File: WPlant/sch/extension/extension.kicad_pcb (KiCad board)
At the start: 2 copper layers, 73 x 50 mm, 45 parts, among them J1 PROG/SWD, J2 HumSnc, J3 HumSnc, J4 HumSnc, J5 HumSnc, J6 Input, J7 Output, J8 LeakDetect, J9 Valves, Q1 FDS9926A, Q2 FDS9926A, U1 PY32F003F18P6TU, U2 74HC594, U3 74HC4052, U4 SP485EEN-L/TR, U6 AP2204R-5.0, U7 SP485EEN-L/TR

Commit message: Update WP Extension and Generic
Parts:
- added C10: 100, Capacitor_THT:CP_Radial_D5.0mm_P2.00mm, F.Cu at (189.5, 61.6)
- added C9: NP, Capacitor_SMD:C_1206_3216Metric_Pad1.33x1.80mm_HandSolder, F.Cu at (191.1, 76.8)
- added R11: 100, Resistor_SMD:R_0603_1608Metric_Pad0.98x0.95mm_HandSolder, F.Cu at (151.1, 62.2)
- moved H4 19.5 mm to (171.6, 61.3)
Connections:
- U3 pad 13: +5V -> Net-(U3-X)
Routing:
- net Net-(U3-X): track 0.00 -> 8.68 mm
- net +9V: track 144.8 -> 148.5 mm
- net /F4: track 22.6 -> 25.2 mm
- net GND: track 69.5 -> 71.7 mm, vias 173 -> 165
- net +5V: track 215.5 -> 214.5 mm
- net /P4: track 23.8 -> 23.3 mm

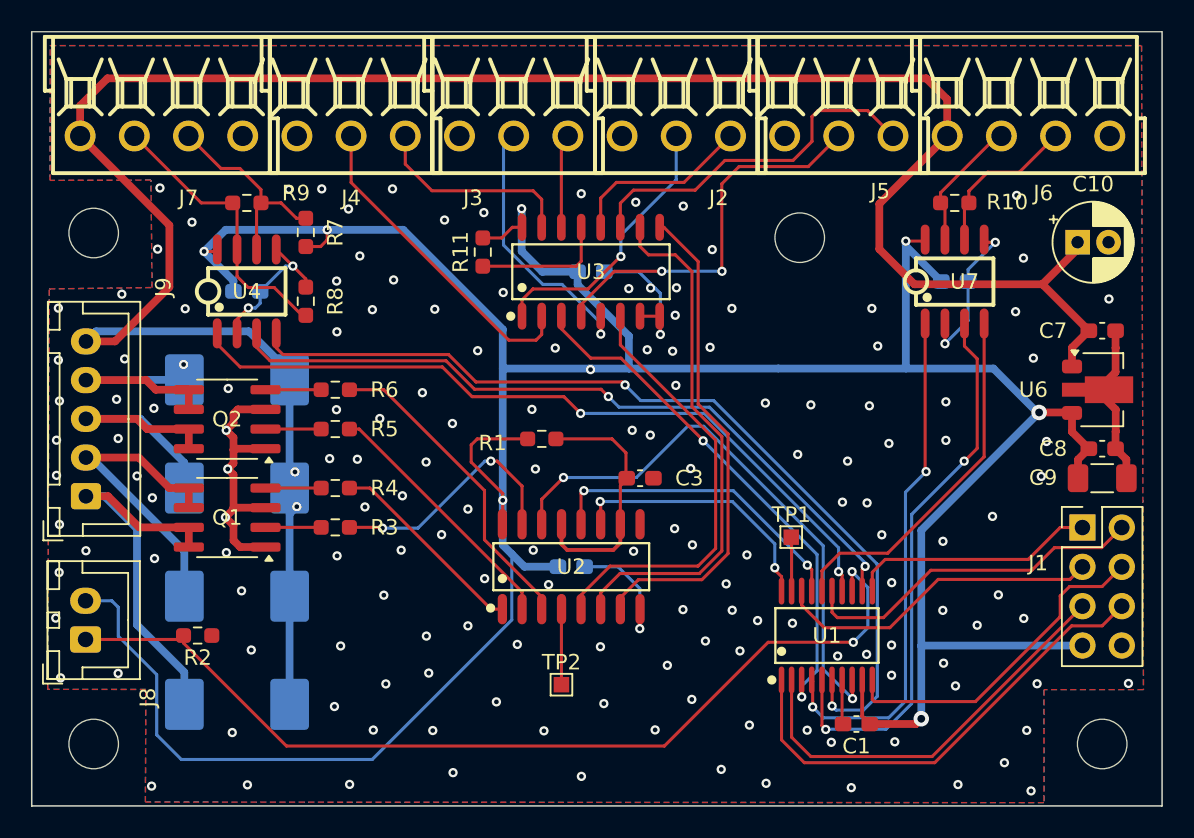
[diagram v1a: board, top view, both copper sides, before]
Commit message: Addeed places for latches on Extension board. Updated MainInt sch and pcb
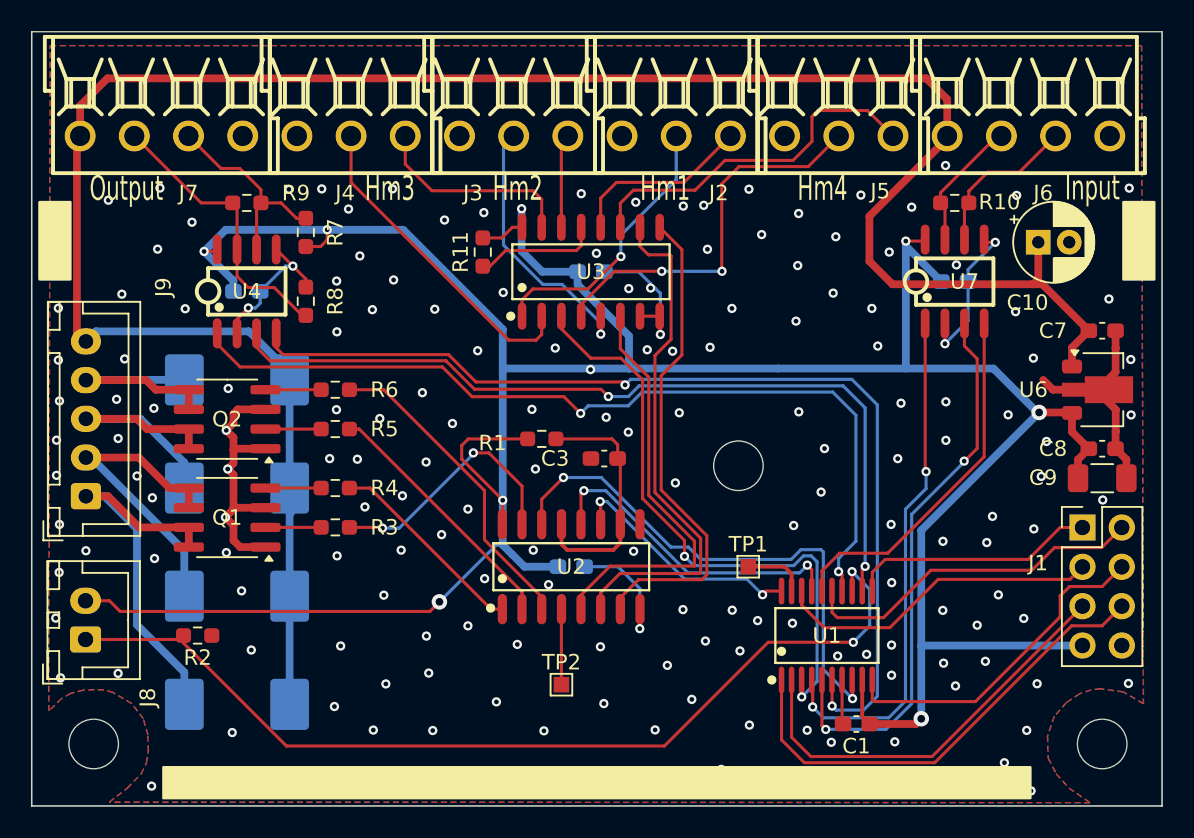
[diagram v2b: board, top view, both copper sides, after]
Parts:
- removed H3: M3, MountingHole:MountingHole_3.2mm_M3
- moved H4 15.3 mm to (167.6, 76.0)
- moved TP1 3.37 mm to (168.3, 82.5)
- moved C3 2.64 mm to (159.0, 75.6), turned to 180 degrees
- moved C10 2.54 mm to (187.0, 61.6)
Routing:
- net +5V: track 214.5 -> 201.2 mm, vias 8 -> 9
- net Net-(U1-PB7): track 49.2 -> 56.9 mm
- net Net-(U1-PB5): track 47.9 -> 54.3 mm
- net Net-(U1-PA7): track 59.2 -> 65.5 mm
- net FREQ-OUT: track 34.1 -> 39.4 mm
- net +9V: track 148.5 -> 143.7 mm, vias 2 -> 0
- net Net-(U1-PA12): track 36.8 -> 34.4 mm
- net GND: track 71.7 -> 73.9 mm, vias 165 -> 179
- net Net-(U1-PA1): track 17.1 -> 15.8 mm
- net Net-(U2-QF): track 28.4 -> 27.1 mm
- net Net-(U3-X): track 8.68 -> 8.11 mm
- net Net-(U1-PA0): track 3.59 -> 4.11 mm
- net Net-(D4-A): vias 1 -> 0
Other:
- board text added: "Hm1"
- board text added: "Hm2"
- board text added: "Hm3"
- board text added: "Hm4"
- board text added: "Input"
- board text added: "Output"

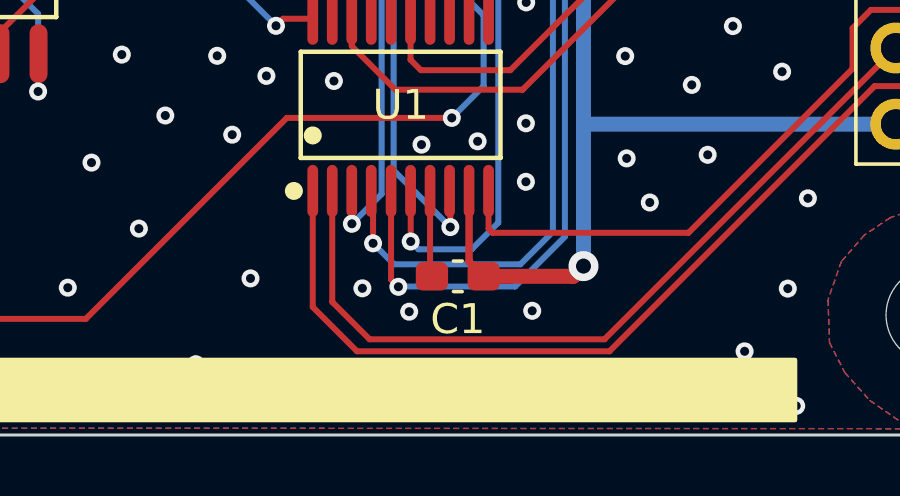
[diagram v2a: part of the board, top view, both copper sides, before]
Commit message: Updated PCB for extension and powermeter
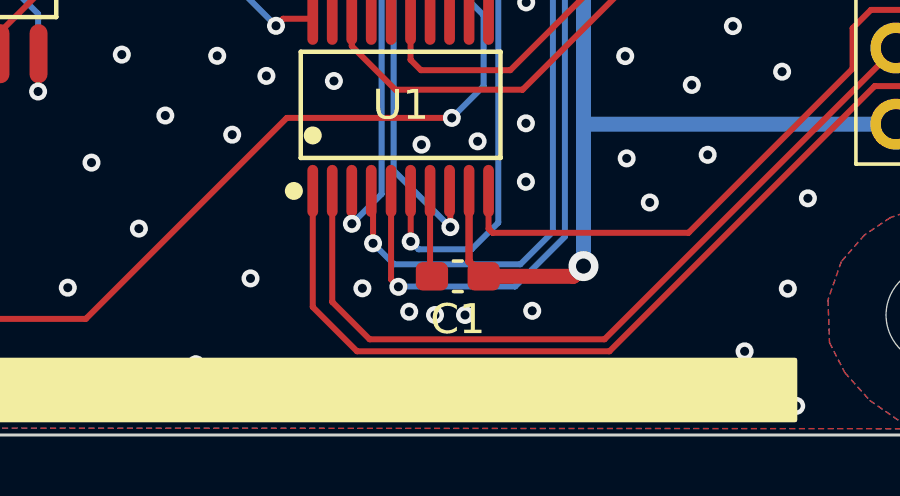
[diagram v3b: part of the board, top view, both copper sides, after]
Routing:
- net GND: vias 179 -> 181
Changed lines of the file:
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@@
+	)
+	(via
+		(at 175.5 94)
+		(size 0.6)
+		(drill 0.3)
+		(layers "F.Cu" "B.Cu")
+		(free yes)
+		(net 1)
 	)
 	(via
@@
 		(size 0.6)
 		(drill 0.3)
+		(layers "F.Cu" "B.Cu")
+		(free yes)
+		(net 1)
+	)
+	(via
+		(at 174.5 94)
+		(size 0.6)
+		(drill 0.3)

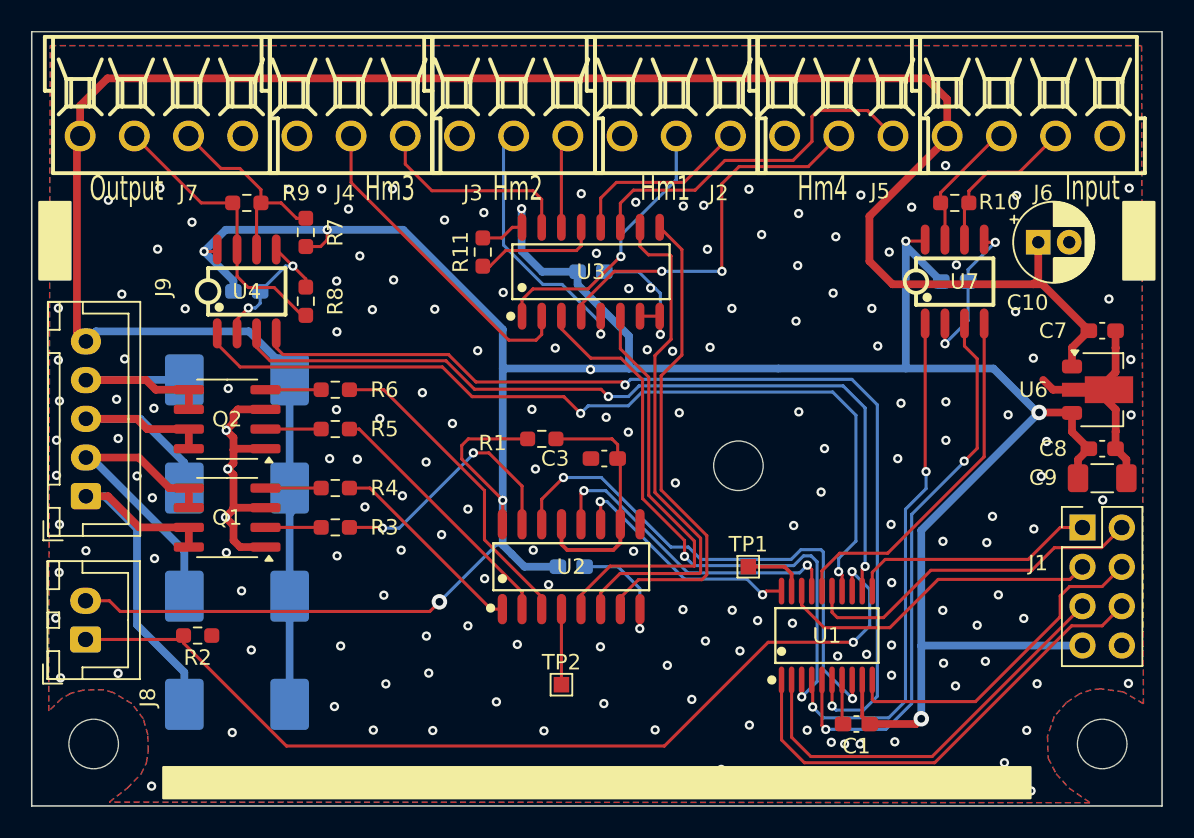
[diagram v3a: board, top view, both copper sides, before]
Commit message: Route of WP project done
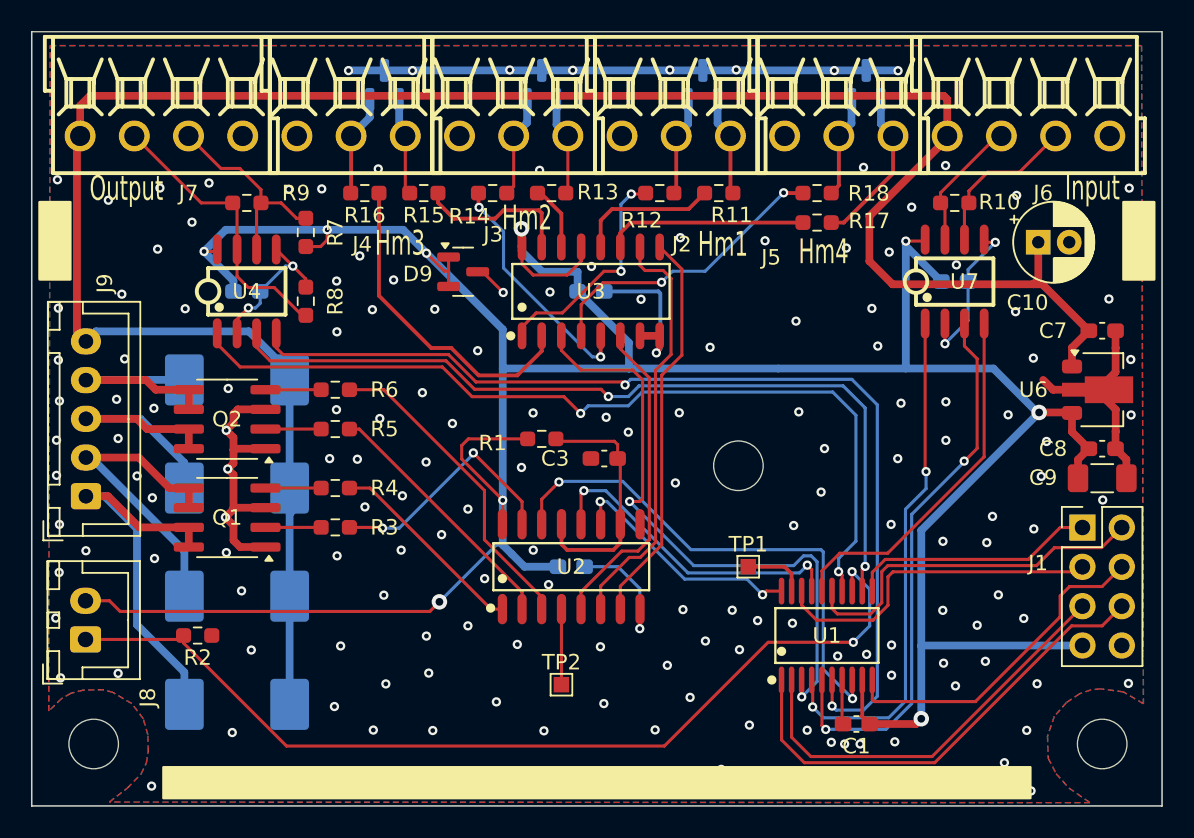
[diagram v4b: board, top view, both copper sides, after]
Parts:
- added D5: MMBZ5V6, Package_TO_SOT_SMD:SOT-23, B.Cu at (175.9, 51.4)
- added D6: MMBZ5V6, Package_TO_SOT_SMD:SOT-23, B.Cu at (144.8, 51.4)
- added D7: MMBZ5V6, Package_TO_SOT_SMD:SOT-23, B.Cu at (154.9, 51.4)
- added D8: MMBZ5V6, Package_TO_SOT_SMD:SOT-23, B.Cu at (165.3, 51.4)
- added D9: MMBZ5V6, Package_TO_SOT_SMD:SOT-23, F.Cu at (149.9, 63.5)
- added R12: 100, Resistor_SMD:R_0603_1608Metric_Pad0.98x0.95mm_HandSolder, F.Cu at (162.6, 58.4)
- added R13: 100, Resistor_SMD:R_0603_1608Metric_Pad0.98x0.95mm_HandSolder, F.Cu at (155.6, 58.4)
- added R14: 100, Resistor_SMD:R_0603_1608Metric_Pad0.98x0.95mm_HandSolder, F.Cu at (151.8, 58.4)
- added R15: 100, Resistor_SMD:R_0603_1608Metric_Pad0.98x0.95mm_HandSolder, F.Cu at (147.3, 58.4)
- added R16: 100, Resistor_SMD:R_0603_1608Metric_Pad0.98x0.95mm_HandSolder, F.Cu at (143.5, 58.4)
- added R17: 100, Resistor_SMD:R_0603_1608Metric_Pad0.98x0.95mm_HandSolder, F.Cu at (172.7, 60.3)
- added R18: 100, Resistor_SMD:R_0603_1608Metric_Pad0.98x0.95mm_HandSolder, F.Cu at (172.7, 58.4)
- moved R11 15.7 mm to (166.4, 58.4), turned to 0 degrees
- moved C4 1.27 mm to (158.1, 64.8)
- moved U3 1.27 mm to (158.1, 64.8)
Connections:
- J2 pad 1: /P1 -> Net-(J2-Pin_1)
- J2 pad 2: /F1 -> Net-(J2-Pin_2)
- J3 pad 1: /P2 -> Net-(J3-Pin_1)
- J3 pad 2: /F2 -> Net-(J3-Pin_2)
- J4 pad 1: /P3 -> Net-(J4-Pin_1)
- J4 pad 2: /F3 -> Net-(J4-Pin_2)
- J5 pad 1: /P4 -> Net-(J5-Pin_1)
- J5 pad 2: /F4 -> Net-(J5-Pin_2)
- R11 pad 1: Net-(U3-X) -> /P1
- R11 pad 2: +5V -> Net-(J2-Pin_1)
- U3 pad 13: Net-(U3-X) -> +5V
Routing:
- net GND: track 73.9 -> 112.4 mm, vias 181 -> 175
- net Net-(J5-Pin_1): track 0.00 -> 10.4 mm
- net /P4: track 23.3 -> 13.0 mm
- net Net-(U3-X): track 8.11 -> 0.00 mm
- net Net-(J3-Pin_2): track 0.00 -> 7.52 mm
- net Net-(J3-Pin_1): track 0.00 -> 7.00 mm
- net Net-(J5-Pin_2): track 0.00 -> 6.59 mm
- net Net-(J4-Pin_2): track 0.00 -> 6.56 mm
- net Net-(J2-Pin_1): track 0.00 -> 6.46 mm
- net Net-(J2-Pin_2): track 0.00 -> 6.43 mm
- net Net-(U2-QG): track 33.6 -> 27.2 mm
- net Net-(J4-Pin_1): track 0.00 -> 6.33 mm
- net Net-(U2-QF): track 27.1 -> 20.9 mm
- net +5V: track 201.2 -> 207.4 mm
- net Net-(U2-QH): track 31.7 -> 25.6 mm
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
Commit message: Added connectors marks on back of PCBs
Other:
- board text added: "+"
- board text added: "-"
- board text added: "1"
- board text added: "2"
- board text added: "3"
- board text added: "4"
- board text added: "A"
- board text added: "B"
- board text added: "In"
- board text added: "Out"

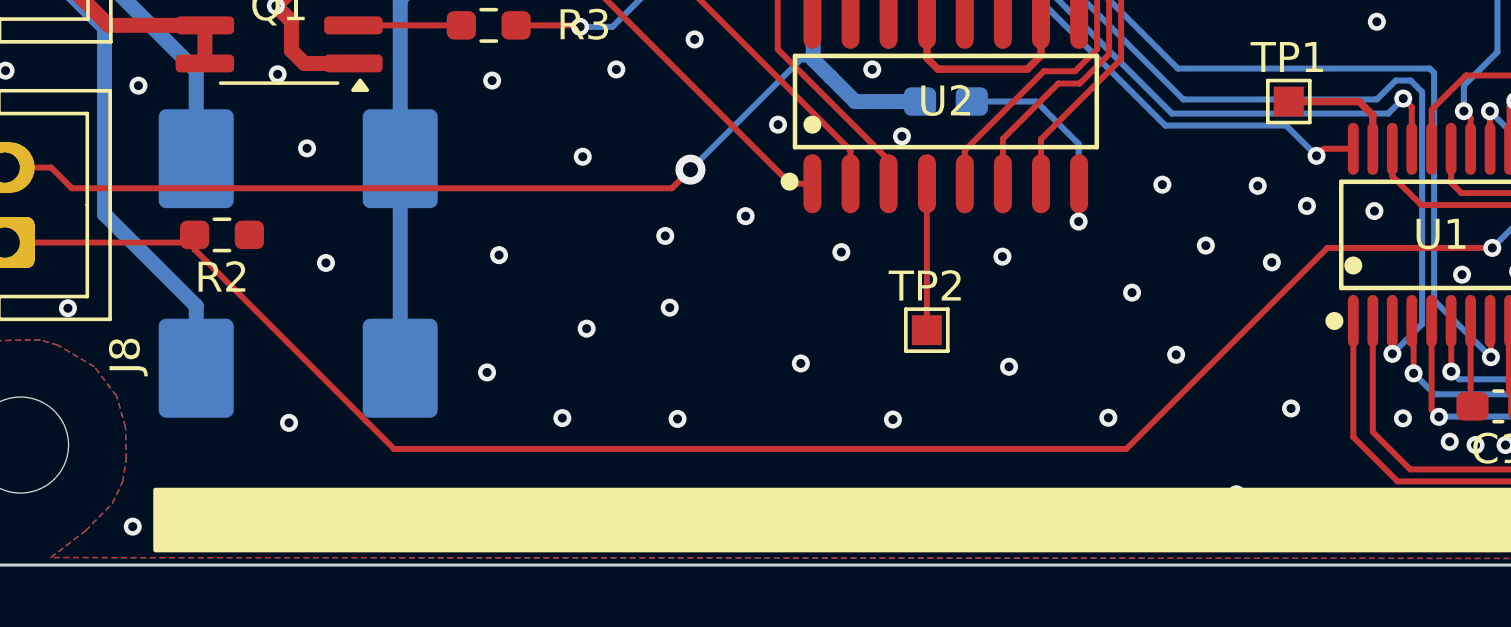
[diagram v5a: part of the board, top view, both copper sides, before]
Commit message: Upate values in SCH of WP
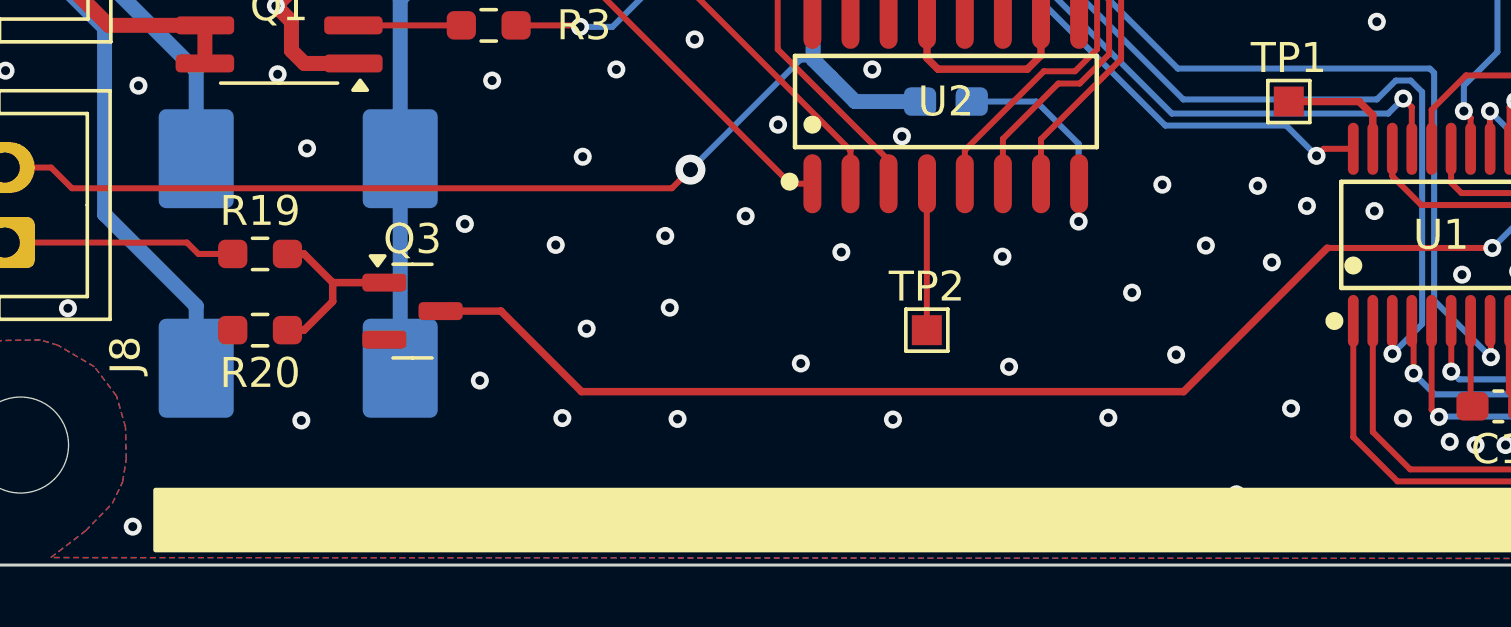
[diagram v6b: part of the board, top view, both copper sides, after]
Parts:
- removed R2: 100K?, Resistor_SMD:R_0603_1608Metric_Pad0.98x0.95mm_HandSolder
- added Q3: S9014, Package_TO_SOT_SMD:SOT-23, F.Cu at (139.1, 89.5)
- added R19: 1K, Resistor_SMD:R_0603_1608Metric_Pad0.98x0.95mm_HandSolder, F.Cu at (134.0, 87.6)
- added R20: 100K, Resistor_SMD:R_0603_1608Metric_Pad0.98x0.95mm_HandSolder, F.Cu at (134.0, 90.2)
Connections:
- U1 pad 13: Net-(J8-Pin_1) -> Net-(Q3-C)
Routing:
- net Net-(J8-Pin_1): track 62.4 -> 7.75 mm, vias 2 -> 0
- net Net-(Q3-C): track 0.00 -> 44.9 mm, vias 0 -> 2
- net Net-(Q3-B): track 0.00 -> 6.16 mm
